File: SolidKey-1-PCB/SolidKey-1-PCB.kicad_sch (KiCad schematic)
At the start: 8 parts, among them J101 USB_C_Receptacle_USB2.0_16P, U101 NCP1117-3.3_SOT223

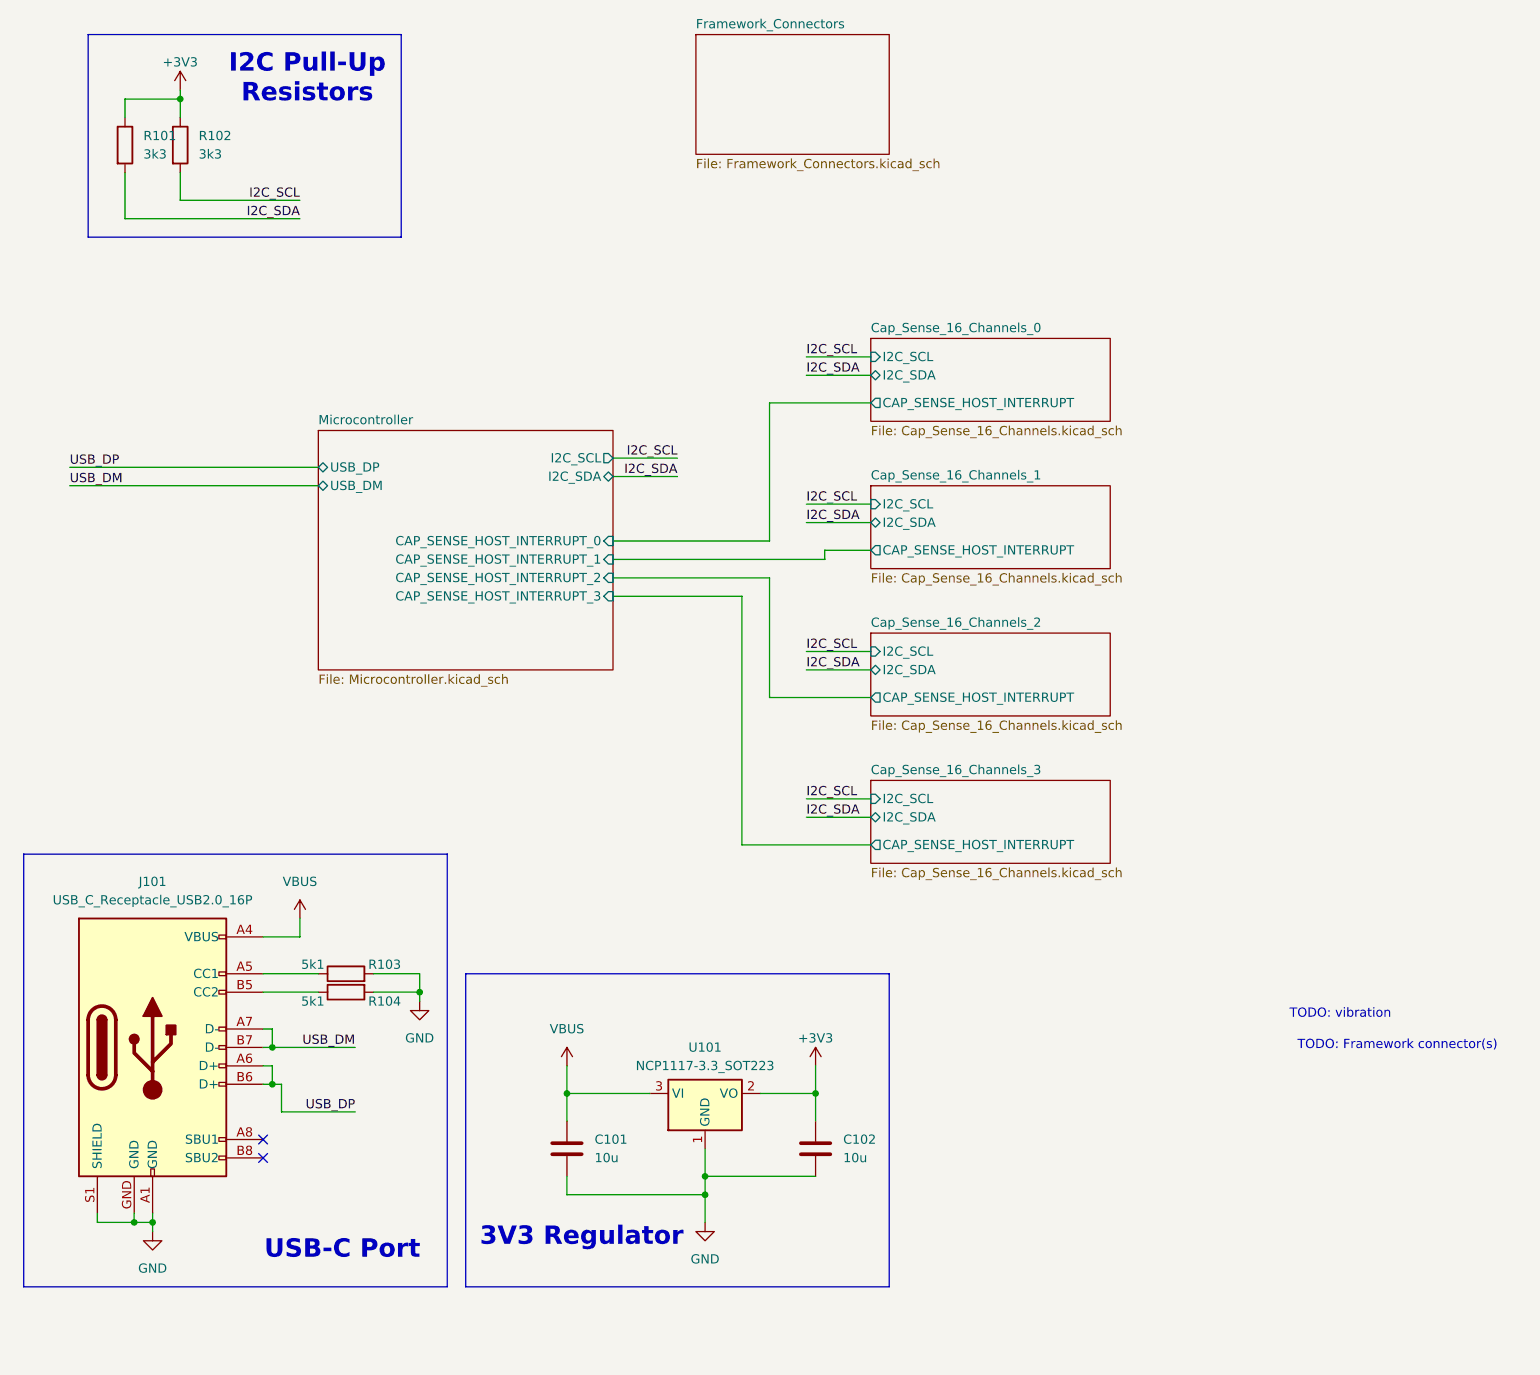
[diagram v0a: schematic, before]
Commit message: Add Framwork connectors and start routing
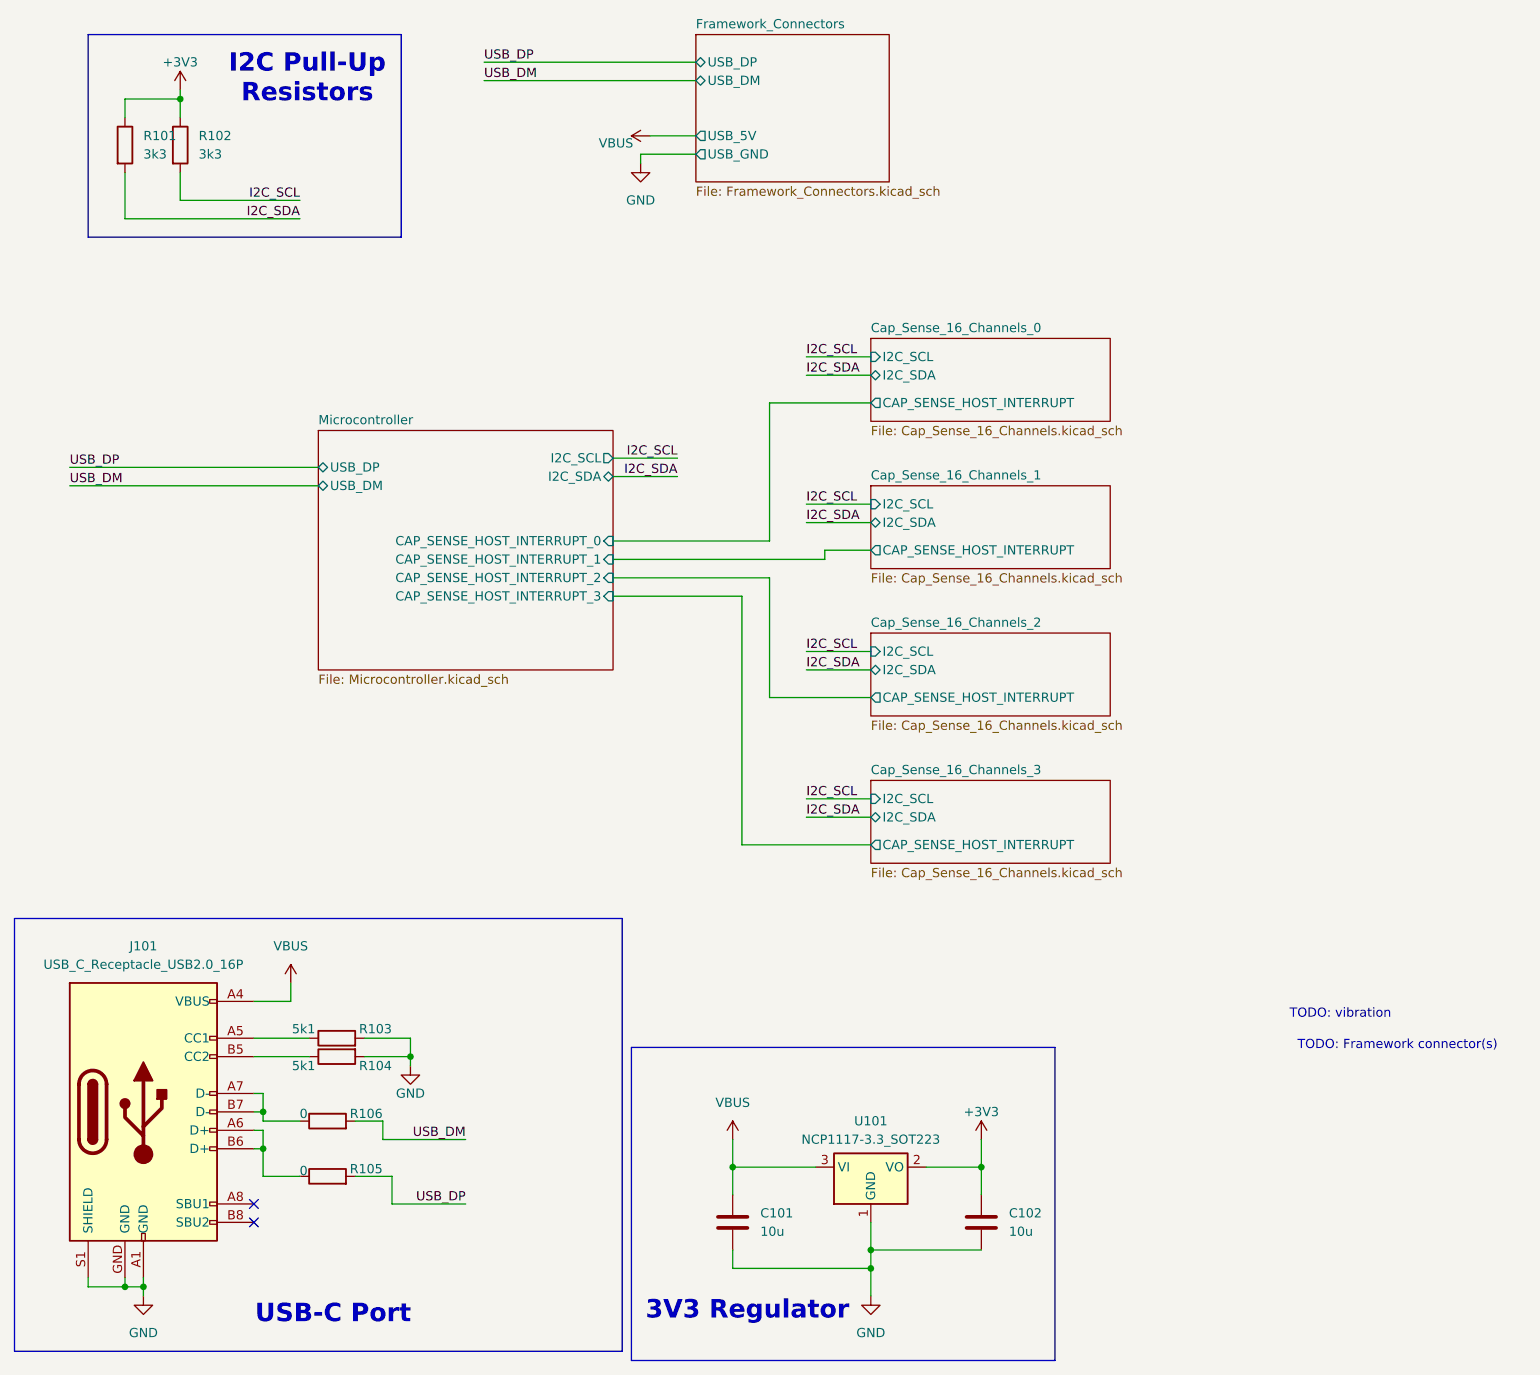
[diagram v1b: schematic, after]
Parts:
- added R105, R106: 0, Resistor_SMD:R_0603_1608Metric, symbol Device:R
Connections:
- net USB_DM: now also R106.2; no longer J101.A7 (D-), J101.B7 (D-)
- net USB_DP: now also R105.2; no longer J101.A6 (D+), J101.B6 (D+)
- new net: J101.A6 (D+), J101.B6 (D+), R105.1
- new net: J101.A7 (D-), J101.B7 (D-), R106.1
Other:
- sheet Framework_Connectors ports: added USB_5V, USB_DM, USB_DP, USB_GND; removed none
- moved on the sheet: C101, C102, J101, R103, R104, U101
